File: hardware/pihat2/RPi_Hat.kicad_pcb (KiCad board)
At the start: 2 copper layers, 65 x 56 mm, 46 parts, among them J2 RPi_GPIO, P1 USB_OTG, P2 BATT, P3 THERM, U1 MCP73833, U2 SMA_Edge_Mount, U3 SMA_Edge_Mount, U4 TPS61027, U5 MCP3021, U6 Si4464, U7 30MHz

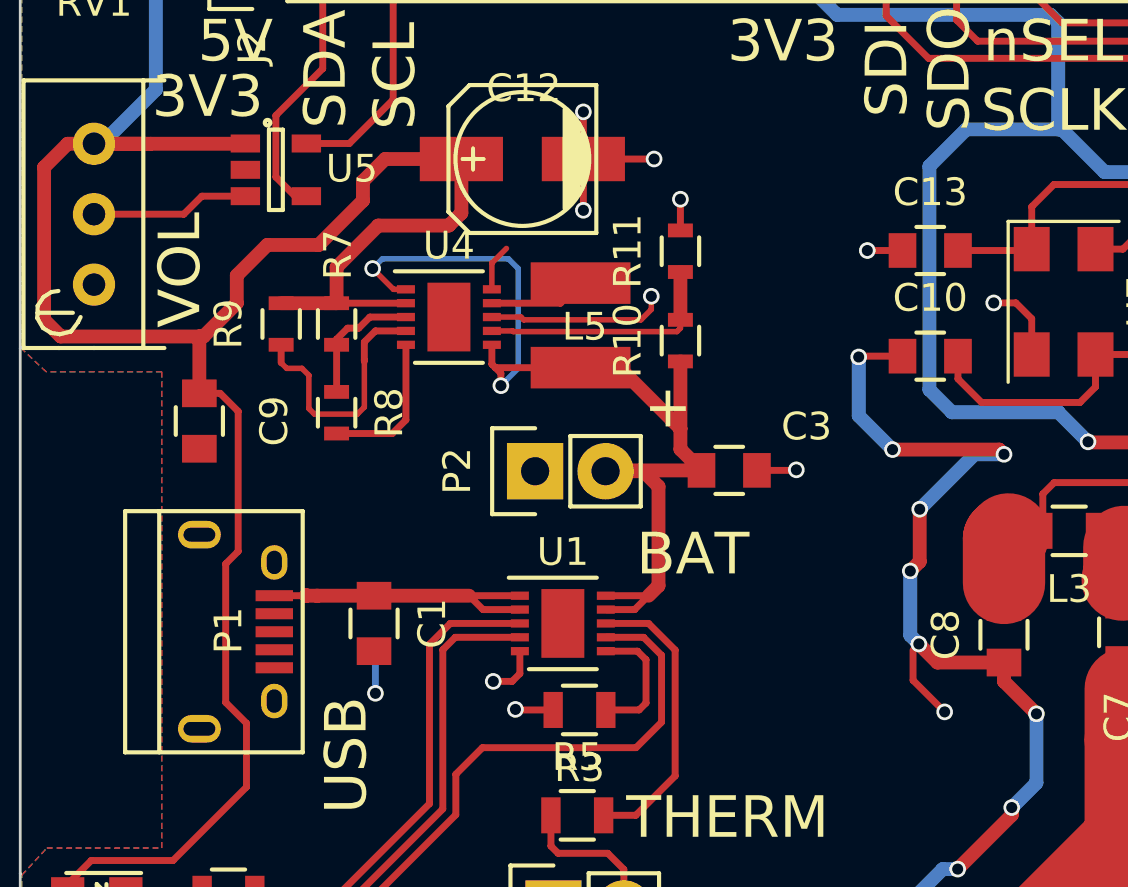
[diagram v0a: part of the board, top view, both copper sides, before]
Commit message: Fixed issues with grounding and trace size.
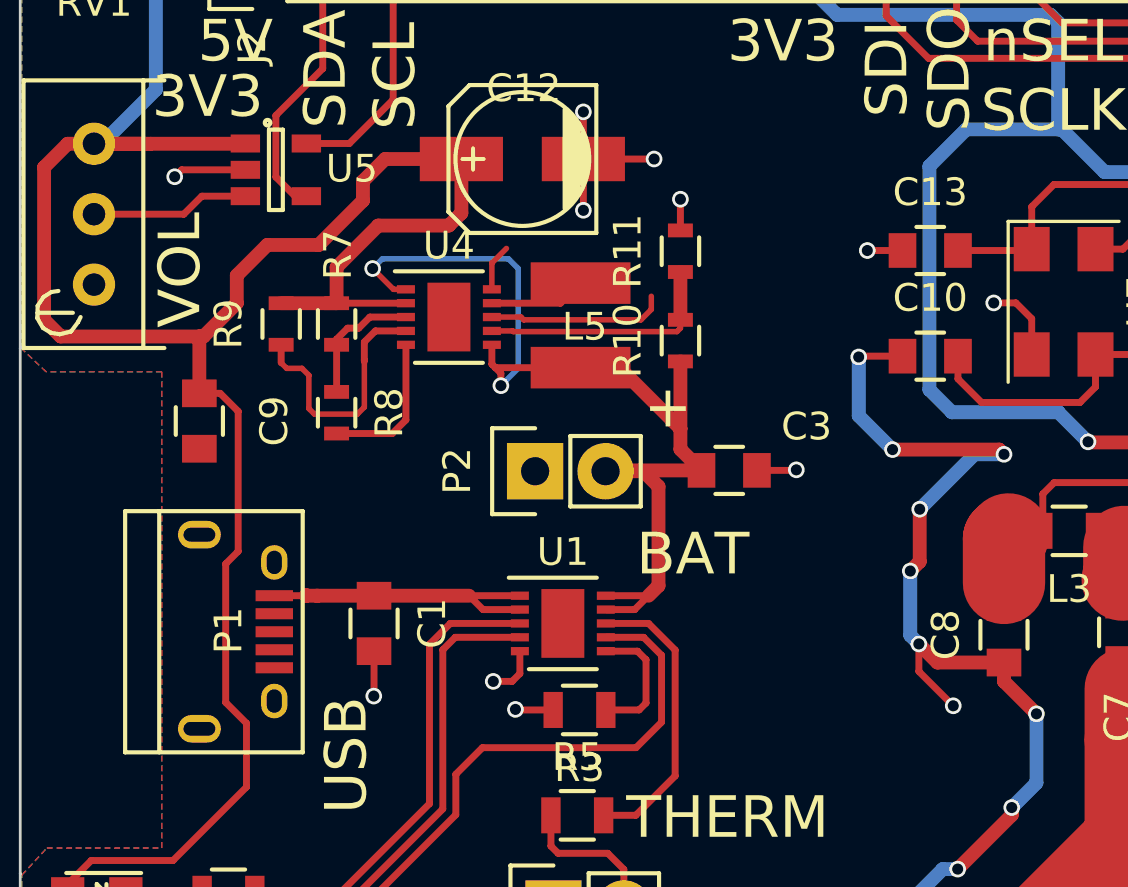
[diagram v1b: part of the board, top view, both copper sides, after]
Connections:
- C1 pad 1: 5VU -> USB_5V
- D1 pad 1: Net-(D1-Pad1) -> (no net)
- D1 pad 2: 5VU -> (no net)
- D2 pad 1: Net-(D2-Pad1) -> (no net)
- D2 pad 2: 5VU -> (no net)
- D3 pad 1: Net-(D3-Pad1) -> (no net)
- D3 pad 2: 5VU -> (no net)
- P1 pad 1: 5VU -> (no net)
- P1 pad 5: GND -> (no net)
- P1 pad 6: GND -> Net-(P1-Pad6)
- R1 pad 1: Net-(D1-Pad1) -> (no net)
- R2 pad 1: Net-(D2-Pad1) -> (no net)
- R4 pad 1: Net-(D3-Pad1) -> (no net)
- RV1 pad 1: GND -> VOL
- RV1 pad 2: VOL -> 5VU
- RV1 pad 3: 5VU -> (no net)
- U1 pad 1: 5VU -> USB_5V
- U1 pad 2: 5VU -> USB_5V
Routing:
- net USB_5V: track 0.00 -> 11.0 mm
- net GND: track 195.5 -> 202.6 mm, vias 57 -> 59
- net 5VU: track 106.1 -> 99.3 mm
- net VOL: track 5.73 -> 1.57 mm
- net (no net): track 4.13 -> 8.25 mm, vias 2 -> 0
- net Net-(D3-Pad1): track 2.75 -> 0.00 mm
- net Net-(D2-Pad1): track 2.75 -> 0.00 mm
- net Net-(D1-Pad1): track 2.75 -> 0.00 mm
